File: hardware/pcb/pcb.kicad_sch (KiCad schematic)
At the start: 48 parts, among them J1 USB_B_Micro, J2 USB_A, J3 USB_A, J4 USB_A, M1 Fan, Q1 S8050, SW1 SW_Push, U1 PCF8574, U2 AT89C52, U3 SL2.1A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

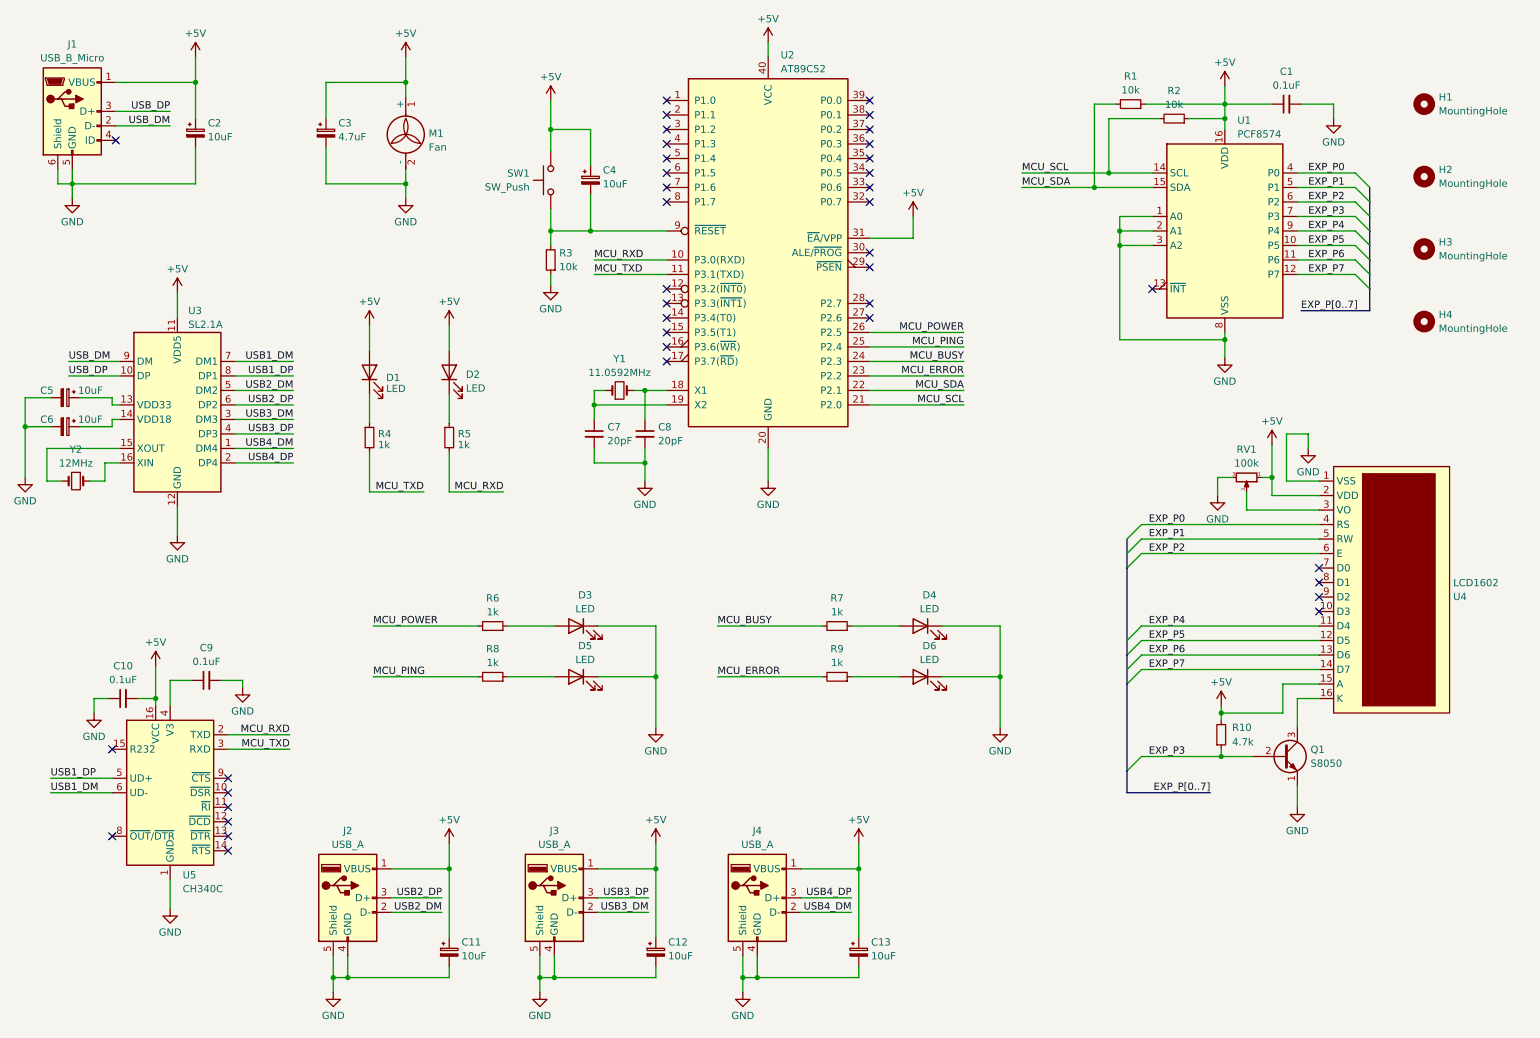
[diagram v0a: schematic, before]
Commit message: Update KiCAD to 8.0
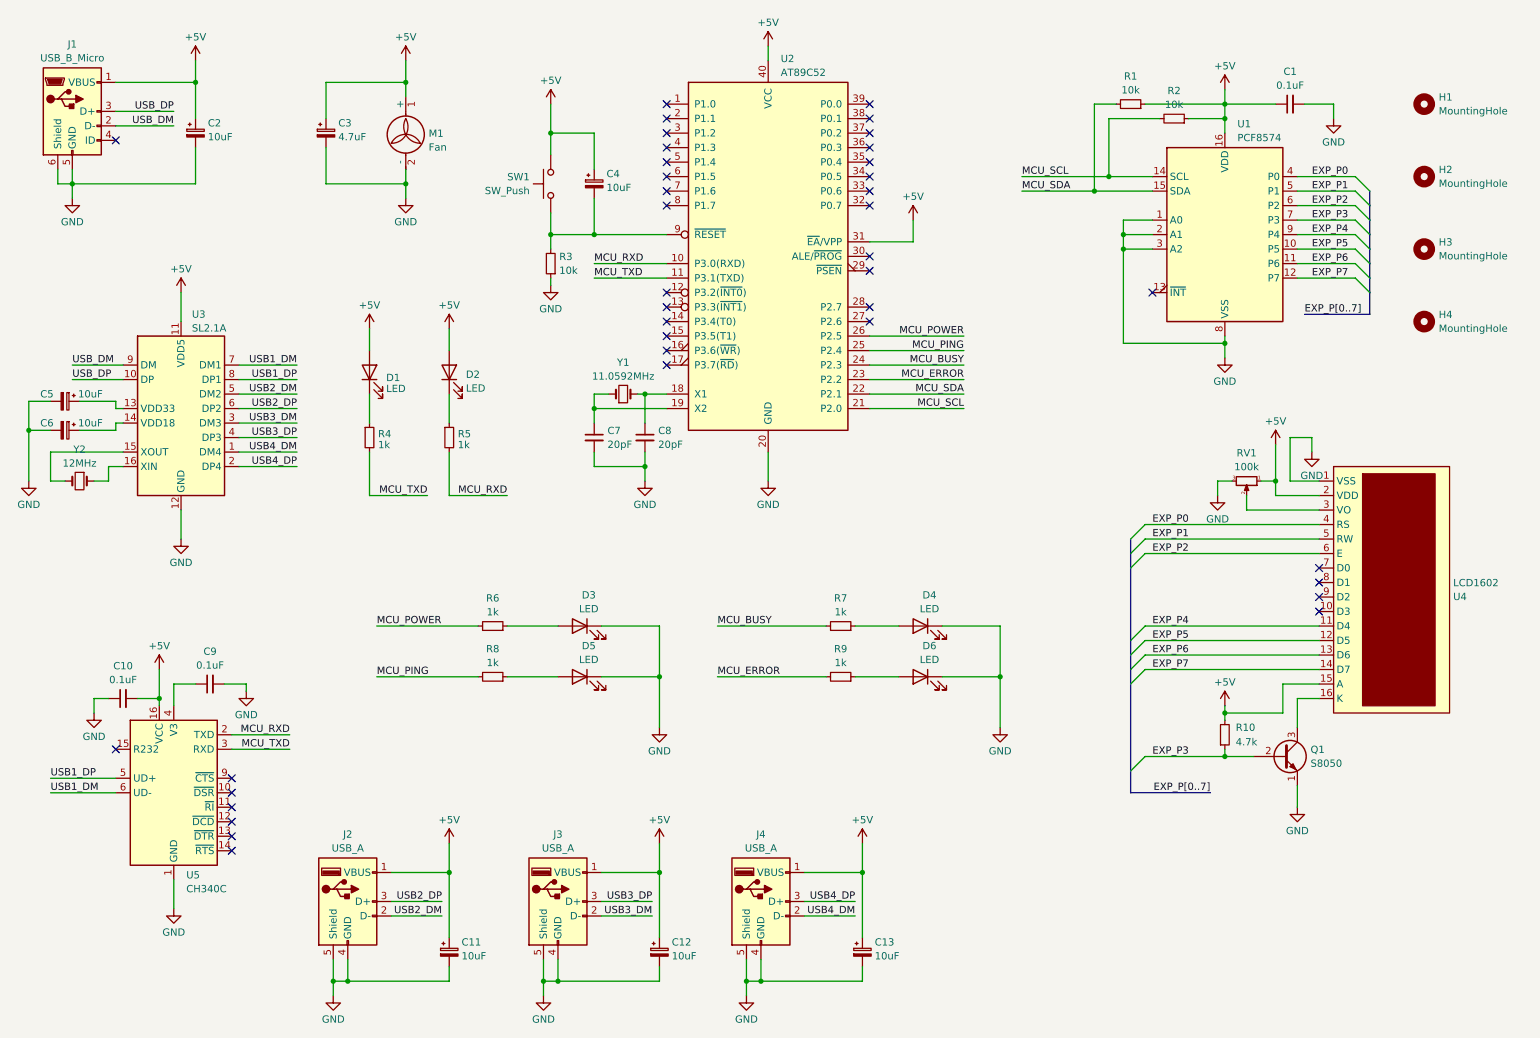
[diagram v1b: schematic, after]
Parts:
- U4: footprint OpenStation:LCD1602 -> Connector_PinSocket_2.54mm:PinSocket_1x16_P2.54mm_Vertical
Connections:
- no-connect marks 40 -> 39
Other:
- moved on the sheet: C1, C12, C13, C4, C5, C6, C7, C8, C9, D3, D5, J2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

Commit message: chore: Update startup message
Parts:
- C7, C8: value 20pF -> 22pF
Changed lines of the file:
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@@
 		(fields_autoplaced yes)
 		(property "Reference" "C7"
-			(at 120.4341 87.6942 0)
-			(effects
-				(font
-					(size 1.27 1.27)
-				)
-				(justify left)
-			)
-		)
-		(property "Value" "20pF"
-			(at 120.4341 90.1184 0)
+			(at 120.65 87.6362 0)
+			(effects
+				(font
+					(size 1.27 1.27)
+				)
+				(justify left)
+			)
+		)
+		(property "Value" "22pF"
+			(at 120.65 90.1762 0)
 			(effects
 				(font
@@
 		(fields_autoplaced yes)
 		(property "Reference" "C8"
-			(at 129.3241 87.6942 0)
-			(effects
-				(font
-					(size 1.27 1.27)
-				)
-				(justify left)
-			)
-		)
-		(property "Value" "20pF"
-			(at 129.3241 90.1184 0)
-			(effects
-				(font
+			(at 129.54 87.6362 0)
+			(effects
+				(font
+					(size 1.27 1.27)
+				)
+				(justify left)
+			)
+		)
+		(property "Value" "22pF"
+			(at 129.54 90.1762 0)
+			(effects
+				(font
